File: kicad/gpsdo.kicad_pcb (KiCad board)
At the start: 2 copper layers, 101.6 x 76.2 mm, 9 parts, among them J1 RJ45_Abracon_ARJP11A-MASA-B-A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, J2 Conn_Coaxial, U1 549CAAC000111BBG, U2 MAX-8Q, U3 Si7051-A20, U4 PIC32MX795F512L-80x-PF

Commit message: add ethernet phy
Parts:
- added C2: 100n, Capacitor_SMD:C_0805_2012Metric, F.Cu at (50.8, 39.4)
- added C3: 100n, Capacitor_SMD:C_0805_2012Metric, F.Cu at (39.7, 45.7)
- added C4: 100n, Capacitor_SMD:C_0805_2012Metric, F.Cu at (108.0, 49.5)
- added C5: 100n, Capacitor_SMD:C_0805_2012Metric, F.Cu at (105.4, 49.5)
- added R2: 100, Resistor_SMD:R_0805_2012Metric, F.Cu at (99.1, 54.6)
- added R3: 100, Resistor_SMD:R_0805_2012Metric, F.Cu at (99.1, 50.8)
- added U5: DP83640TVV_NOPB, Package_QFP:LQFP-48_7x7mm_P0.5mm, F.Cu at (86.4, 50.8)
- moved U1 16.9 mm to (51.2, 45.7)
- moved U3 16.9 mm to (45.7, 45.7)
- moved U4 14.8 mm to (64.8, 76.2), turned to 90 degrees
- renumbered C2 to C1
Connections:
- J1 pad 1: Net-(J1-Pad1) -> TD+
- J1 pad 2: Net-(J1-Pad2) -> TD-
- J1 pad 3: Net-(J1-Pad3) -> RD+
- J1 pad 4: Net-(J1-Pad4) -> +3V3
- J1 pad 5: Net-(J1-Pad5) -> +3V3
- J1 pad 6: Net-(J1-Pad6) -> RD-
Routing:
- net RD-: track 0.00 -> 29.3 mm, vias 0 -> 1
- net TD+: track 0.00 -> 26.7 mm, vias 0 -> 2
- net TD-: track 0.00 -> 25.4 mm
- net RD+: track 0.00 -> 21.6 mm
- net +3V3: track 0.00 -> 9.55 mm
- net GND: track 0.00 -> 6.49 mm, vias 43 -> 68

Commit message: board progress
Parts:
- removed the U4 at (64.8, 76.2)
- added R10: 10k, Resistor_SMD:R_0603_1608Metric, F.Cu at (56.0, 78.1)
- added R11: 10k, Resistor_SMD:R_0603_1608Metric, F.Cu at (52.6, 78.1)
- added R12: 10k, Resistor_SMD:R_0603_1608Metric, F.Cu at (56.0, 80.0)
- added R13: 10k, Resistor_SMD:R_0603_1608Metric, F.Cu at (52.6, 80.0)
- added R14: 10k, Resistor_SMD:R_0603_1608Metric, F.Cu at (56.0, 81.9)
- added R15: 10k, Resistor_SMD:R_0603_1608Metric, F.Cu at (52.6, 81.9)
- added R16: 10k, Resistor_SMD:R_0603_1608Metric, F.Cu at (56.0, 83.8)
- added R17: 10k, Resistor_SMD:R_0603_1608Metric, F.Cu at (52.6, 83.8)
- added R18: 10k, Resistor_SMD:R_0603_1608Metric, F.Cu at (56.0, 85.7)
- added R19: 10k, Resistor_SMD:R_0603_1608Metric, F.Cu at (52.6, 85.7)
- added R4: 10k, Resistor_SMD:R_0603_1608Metric, F.Cu at (56.0, 72.4)
- added R5: 10k, Resistor_SMD:R_0603_1608Metric, F.Cu at (52.6, 72.4)
- added R6: 10k, Resistor_SMD:R_0603_1608Metric, F.Cu at (56.0, 74.3)
- added R7: 10k, Resistor_SMD:R_0603_1608Metric, F.Cu at (52.6, 74.3)
- added R8: 10k, Resistor_SMD:R_0603_1608Metric, F.Cu at (56.0, 76.2)
- added R9: 10k, Resistor_SMD:R_0603_1608Metric, F.Cu at (52.6, 76.2)
- added U5: AM3352BZCE60, kicad:BGA298C65P19X19_1300X1300X130, F.Cu at (67.3, 67.3)
- moved C4 7.11 mm to (56.1, 44.1), turned to 270 degrees
- moved C5 6.90 mm to (45.7, 49.1)
- renumbered C4 to C2, C5 to C3, C2 to C4, C3 to C5, J2 to J1, J1 to J2, U3 to U2, U2 to U3, U5 to U4
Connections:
- net Net-(U1-Pad4) renamed CLK_25M
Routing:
- net Net-(U1-Pad7): track 0.00 -> 5.85 mm
- net Net-(U1-Pad8): track 0.00 -> 5.85 mm
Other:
- copper layers 2 -> 4
- rule trace_min: 0.2 -> 0.127
- rule via_min_drill: 0.3 -> 0.254
- rule via_min_size: 0.4 -> 0.508

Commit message: update layout
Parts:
- removed the C3 at (105.4, 49.5)
- removed J2: RJ45_Abracon_ARJP11A-MASA-B-A-EMU2, Connector_RJ:RJ45_Abracon_ARJP11A-MA_Horizontal
- removed R10, R11, R12, R13, R14, R15, R16, R17, R18, R19, R4, R5, R6, R7, R8, R9: 10k, Resistor_SMD:R_0603_1608Metric
- removed R2, R3: 100, Resistor_SMD:R_0805_2012Metric
- removed the U3 at (105.3, 79.2)
- removed the U4 at (86.4, 50.8)
- removed U5: AM3352BZCE60, kicad:BGA298C65P19X19_1300X1300X130
- added C5: 100n, Capacitor_SMD:C_0805_2012Metric, F.Cu at (81.3, 45.5)
- added C6: 100n, Capacitor_SMD:C_0805_2012Metric, F.Cu at (85.7, 42.5)
- added C7: 470n, Capacitor_SMD:C_0805_2012Metric, F.Cu at (81.3, 48.4)
- added U1: MSP430F5171IDA, Package_SO:TSSOP-38_4.4x9.7mm_P0.5mm, F.Cu at (74.9, 46.7)
- added U2: MAX-8Q, RF_GPS:ublox_MAX, F.Cu at (105.3, 36.6)
- moved C1 42.5 mm to (116.8, 35.2)
- moved J1 42.5 mm to (122.3, 39.9)
- moved L1 42.5 mm to (116.8, 39.0)
- moved R1 42.5 mm to (114.6, 37.1)
- moved C2 27.6 mm to (81.3, 42.5), turned to 0 degrees
- renumbered C4 to C3, C5 to C4, U1 to U3, U2 to U4
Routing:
- net RD-: track 29.3 -> 0.00 mm, vias 1 -> 0
- net TD+: track 26.7 -> 0.00 mm, vias 2 -> 0
- net TD-: track 25.4 -> 0.00 mm
- net RD+: track 21.6 -> 0.00 mm
- net +3V3: track 9.55 -> 0.00 mm
- net GND: track 6.49 -> 0.00 mm, vias 68 -> 43

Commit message: update layout
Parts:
- added J2: Conn_01x04_Male, Connector_PinHeader_2.54mm:PinHeader_1x04_P2.54mm_Vertical, F.Cu at (27.9, 27.9)
- added J3: Conn_01x04_Male, Connector_PinHeader_2.54mm:PinHeader_1x04_P2.54mm_Vertical, F.Cu at (46.6, 69.8)
- added J4: Conn_01x04_Male, Connector_PinHeader_2.54mm:PinHeader_1x04_P2.54mm_Vertical, F.Cu at (51.2, 69.8)
- added J5: Conn_01x04_Male, Connector_PinHeader_2.54mm:PinHeader_1x04_P2.54mm_Vertical, F.Cu at (55.9, 69.8)
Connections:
- U1 pad 15: Net-(U1-Pad15) -> gPPS
- U2 pad 4: Net-(U2-Pad4) -> gPPS

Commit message: update board layout
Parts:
- added C10: 10u, Capacitor_SMD:C_0805_2012Metric, F.Cu at (53.9, 34.0)
- added C11: 100n, Resistor_SMD:R_0603_1608Metric, F.Cu at (73.7, 38.1)
- added C8: 100n, Resistor_SMD:R_0603_1608Metric, F.Cu at (73.9, 53.3)
- added C9: 100n, Resistor_SMD:R_0603_1608Metric, F.Cu at (54.1, 30.5)
- added R2: 1.5k, Resistor_SMD:R_0603_1608Metric, F.Cu at (66.8, 44.7)
- added R3: 1.5k, Resistor_SMD:R_0603_1608Metric, F.Cu at (66.8, 46.7)
- added R4: 1.5k, Resistor_SMD:R_0603_1608Metric, F.Cu at (88.7, 31.7)
- added R5: 1.5k, Resistor_SMD:R_0603_1608Metric, F.Cu at (90.4, 31.7)
- added R6: 1.5k, Resistor_SMD:R_0603_1608Metric, F.Cu at (49.8, 42.4)
- added R7: 1.5k, Resistor_SMD:R_0603_1608Metric, F.Cu at (49.8, 38.3)
- added U5: LTC4317, Package_DFN_QFN:DFN-16-1EP_3x5mm_P0.5mm_EP1.66x4.4mm, F.Cu at (73.7, 50.3)
- C1, C2, C3, C4, C5, C6: footprint Capacitor_SMD:C_0805_2012Metric -> Resistor_SMD:R_0603_1608Metric
- L1: footprint Inductor_SMD:L_0805_2012Metric -> Resistor_SMD:R_0603_1608Metric
- R1: footprint Resistor_SMD:R_0805_2012Metric -> Resistor_SMD:R_0603_1608Metric
- moved J5 55.0 mm to (91.4, 27.9), turned to 90 degrees
- moved J4 43.5 mm to (91.4, 53.3), turned to 90 degrees
- moved C6 25.9 mm to (60.2, 38.3), turned to 90 degrees
- moved J1 25.4 mm to (96.8, 39.9)
- moved R1 24.4 mm to (90.2, 36.1), turned to 180 degrees
- moved L1 23.9 mm to (93.0, 39.0)
- moved U2 23.9 mm to (81.4, 36.6)
- moved C1 23.9 mm to (93.0, 35.2)
- moved C7 23.3 mm to (66.9, 30.1), turned to 90 degrees
- moved J2 22.4 mm to (50.3, 27.9)
- moved C2 20.3 mm to (65.0, 30.3), turned to 90 degrees
- moved C5 18.7 mm to (70.3, 30.3), turned to 90 degrees
- moved C3 17.4 mm to (40.9, 35.6), turned to 0 degrees
- moved J3 16.9 mm to (50.3, 53.3), turned to 90 degrees
- moved U1 13.6 mm to (66.3, 36.2), turned to 90 degrees
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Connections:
- net Net-(U1-Pad16) renamed oPPS
- J2 pad 3: GND -> +3V3
- J2 pad 4: GND -> ePPS
- J4 pad 1: GND -> Net-(J4-Pad1)
- J4 pad 2: GND -> Net-(J4-Pad2)
- J5 pad 1: GND -> Net-(J5-Pad1)
- J5 pad 2: GND -> Net-(J5-Pad2)
- U1 pad 17: Net-(U1-Pad17) -> ePPS
- U1 pad 6: Net-(U1-Pad6) -> Net-(J4-Pad1)
- U1 pad 7: Net-(U1-Pad7) -> Net-(J4-Pad2)
- U2 pad 16: Net-(U2-Pad16) -> Net-(R5-Pad1)
- U2 pad 17: Net-(U2-Pad17) -> Net-(R4-Pad2)
- U2 pad 2: Net-(U2-Pad2) -> Net-(J5-Pad1)
- U2 pad 3: Net-(U2-Pad3) -> Net-(J5-Pad2)
- U2 pad 9: Net-(U2-Pad9) -> Net-(U1-Pad19)
- U3 pad 1: Net-(U3-Pad1) -> +3V3
- U3 pad 7: Net-(U2-Pad16) -> Net-(R7-Pad1)
- U3 pad 8: Net-(U2-Pad17) -> Net-(R6-Pad2)
- U4 pad 1: Net-(U2-Pad16) -> Net-(R7-Pad1)
- U4 pad 4: Net-(U4-Pad4) -> +3V3
- U4 pad 6: Net-(U2-Pad17) -> Net-(R6-Pad2)
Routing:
- net Net-(R7-Pad1): track 0.00 -> 46.7 mm, vias 0 -> 4
- net Net-(R6-Pad2): track 0.00 -> 45.2 mm, vias 0 -> 4
- net Net-(J4-Pad2): track 0.00 -> 42.5 mm
- net Net-(J4-Pad1): track 0.00 -> 40.2 mm
- net GND: track 0.00 -> 36.5 mm, vias 43 -> 33
- net Net-(R4-Pad2): track 0.00 -> 29.6 mm, vias 0 -> 2
- net Net-(R5-Pad1): track 0.00 -> 25.3 mm
- net CLK_25M: track 0.00 -> 24.2 mm
- net Net-(U1-Pad23): track 0.00 -> 22.5 mm, vias 0 -> 2
- net Net-(U1-Pad24): track 0.00 -> 22.3 mm, vias 0 -> 2
- net Net-(J5-Pad2): track 0.00 -> 20.5 mm
- net ePPS: track 0.00 -> 19.9 mm, vias 0 -> 4
- net Net-(R3-Pad1): track 0.00 -> 19.8 mm
- net Net-(J5-Pad1): track 0.00 -> 17.0 mm
- net Net-(R2-Pad2): track 0.00 -> 16.7 mm, vias 0 -> 2
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- added copper zone on F.Cu, net +3V3
- removed copper zone on F.Cu, net GND
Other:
- board size 101.6 x 76.2 mm -> 76.2 x 30.5 mm
- copper layers 4 -> 2

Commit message: update pcb layout
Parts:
- added C12: 100n, Resistor_SMD:R_0603_1608Metric, F.Cu at (57.1, 48.7)
- added C13: 100n, Resistor_SMD:R_0603_1608Metric, F.Cu at (62.2, 48.8)
- added C14: 100n, Resistor_SMD:R_0603_1608Metric, F.Cu at (52.1, 48.7)
- added C15: 100n, Resistor_SMD:R_0603_1608Metric, F.Cu at (57.4, 38.3)
- added J6: Conn_01x04_Male, Connector_PinHeader_2.54mm:PinHeader_1x04_P2.54mm_Vertical, F.Cu at (74.4, 27.9)
- added R8: 15k, Resistor_SMD:R_0603_1608Metric, F.Cu at (54.6, 45.0)
- added R9: 15k, Resistor_SMD:R_0603_1608Metric, F.Cu at (59.7, 45.0)
- added U10: 74AUC1G79, Package_TO_SOT_SMD:SOT-23-5, F.Cu at (72.4, 43.4)
- added U6: 74LVC1G08, Package_TO_SOT_SMD:SOT-23-5, F.Cu at (59.7, 48.4)
- added U7: 74LVC1G08, Package_TO_SOT_SMD:SOT-23-5, F.Cu at (54.6, 48.4)
- added U8: 74AUC1G79, Package_TO_SOT_SMD:SOT-23-5, F.Cu at (49.5, 48.4)
- added U9: 74LVC1G86, Package_TO_SOT_SMD:SOT-23-5, F.Cu at (54.7, 38.1)
- moved C10 34.8 mm to (85.9, 47.8)
- moved R7 0.81 mm to (49.8, 39.1)
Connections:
- net Net-(J4-Pad1) renamed /uTXD
- net Net-(J4-Pad2) renamed /uRXD
- net Net-(J5-Pad1) renamed /gTXD
- net Net-(J5-Pad2) renamed /gRXD
- net Net-(R2-Pad2) renamed /SCL
- net Net-(R3-Pad1) renamed /SDA
- net Net-(R4-Pad2) renamed /SCL2
- net Net-(R5-Pad1) renamed /SDA2
- net Net-(R6-Pad2) renamed /SCL1
- net Net-(R7-Pad1) renamed /SDA1
- J2 pad 4: ePPS -> +3V3
- J3 pad 3: GND -> /CLK
- J3 pad 4: GND -> /PPS
- U1 pad 15: gPPS -> oPPS
- U1 pad 16: oPPS -> gPPS
- U1 pad 17: ePPS -> Net-(U1-Pad17)
- U1 pad 18: Net-(U1-Pad18) -> dPPS
- U1 pad 23: Net-(U1-Pad23) -> /EN2
- U1 pad 24: Net-(U1-Pad24) -> /EN1
- U1 pad 25: Net-(U1-Pad25) -> iPPS
- U1 pad 26: Net-(U1-Pad26) -> mPPS
- U1 pad 27: Net-(U1-Pad27) -> gPPS
- U1 pad 35: Net-(U1-Pad35) -> /SBWTCK
- U1 pad 36: Net-(U1-Pad36) -> /SBWTDIO
- U1 pad 5: Net-(U1-Pad5) -> EN_CLK
- U1 pad 8: Net-(U1-Pad8) -> EN_PPS
- U5 pad 2: Net-(U1-Pad23) -> /EN1
- U5 pad 8: Net-(U1-Pad24) -> /EN2
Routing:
- net oPPS: track 0.00 -> 42.8 mm, vias 0 -> 2
- net /SBWTDIO: track 0.00 -> 22.7 mm
- net Net-(U1-Pad23): track 22.5 -> 0.00 mm, vias 2 -> 0
- net Net-(U1-Pad24): track 22.3 -> 0.00 mm, vias 2 -> 0
- net /EN1: track 0.00 -> 21.8 mm, vias 0 -> 2
- net /EN2: track 0.00 -> 21.8 mm, vias 0 -> 2
- net ePPS: track 19.9 -> 0.00 mm, vias 4 -> 0
- net /SBWTCK: track 0.00 -> 19.2 mm
- net mPPS: track 0.00 -> 15.7 mm
- net iPPS: track 0.00 -> 15.3 mm
- net EN_CLK: track 0.00 -> 14.8 mm
- net EN_PPS: track 0.00 -> 12.8 mm, vias 0 -> 2
- net gPPS: track 10.3 -> 21.3 mm, vias 0 -> 2
- net CLK_25M: track 24.2 -> 34.5 mm
- net GND: track 36.5 -> 46.5 mm, vias 33 -> 42
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
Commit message: create gerber files
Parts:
- added R10: 47k, Resistor_SMD:R_0603_1608Metric, F.Cu at (64.0, 26.7)
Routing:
- net /SBWTDIO: track 22.7 -> 23.4 mm

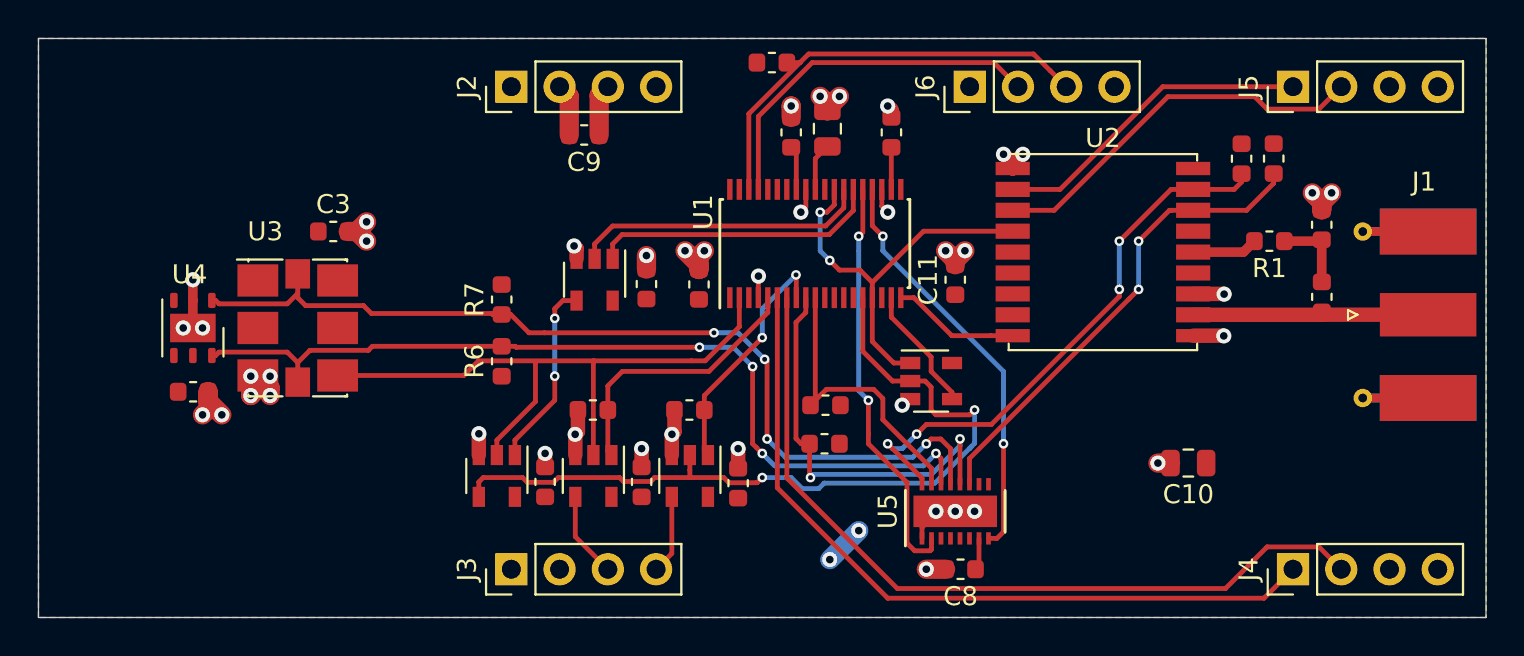
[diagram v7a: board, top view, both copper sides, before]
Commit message: add DCXO shield
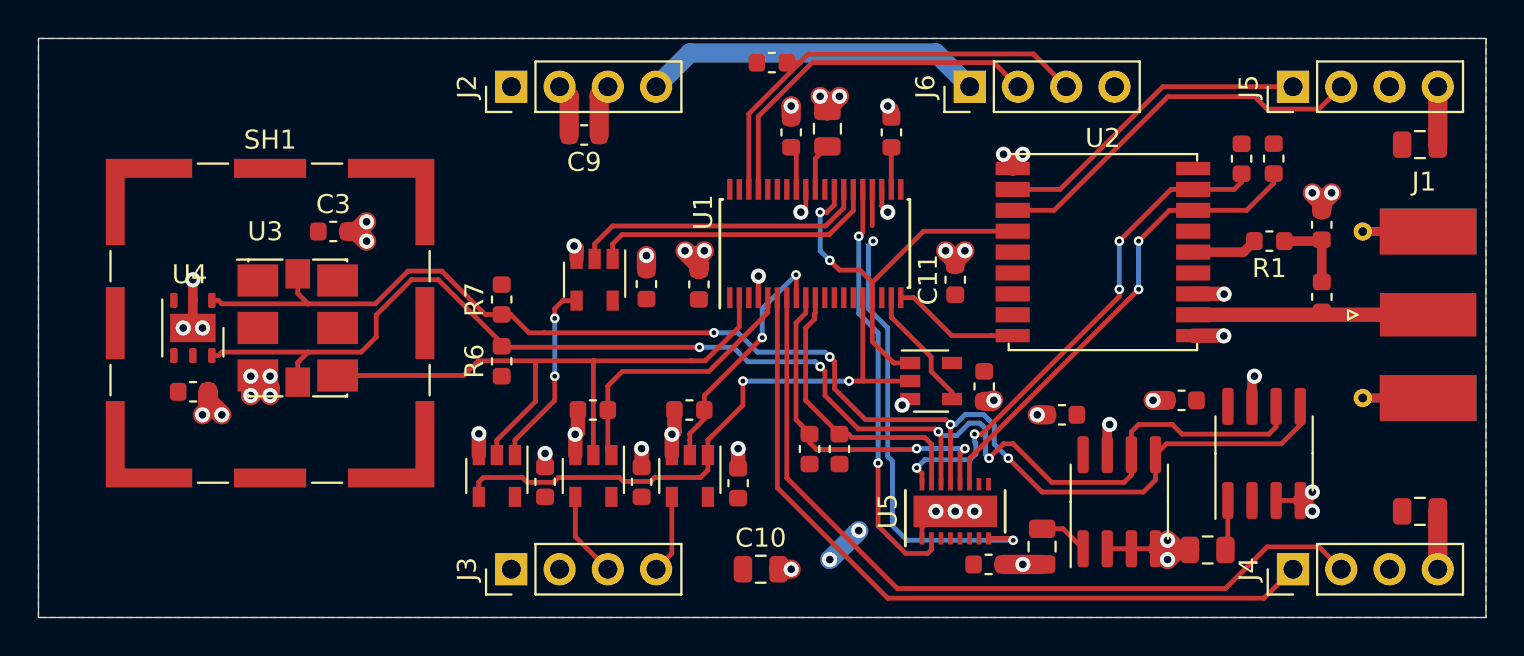
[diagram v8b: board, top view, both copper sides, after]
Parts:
- added C16: 100n, Resistor_SMD:R_0603_1608Metric, F.Cu at (85.6, 44.5)
- added C17: 100n, Resistor_SMD:R_0603_1608Metric, F.Cu at (75.2, 43.7)
- added C18: 100n, Resistor_SMD:R_0603_1608Metric, F.Cu at (79.3, 45.2)
- added C19: 10u, Capacitor_SMD:C_0805_2012Metric, F.Cu at (98.1, 50.3)
- added C20: 10u, Capacitor_SMD:C_0805_2012Metric, F.Cu at (98.1, 31.0)
- added C21: 22u, Capacitor_SMD:C_0805_2012Metric, F.Cu at (78.2, 52.1)
- added C22: 22u, Capacitor_SMD:C_0805_2012Metric, F.Cu at (86.9, 52.3)
- added SH1: DCXO Shield, RF_Shielding:Laird_Technologies_BMI-S-102_16.50x16.50mm, F.Cu at (37.6, 40.4)
- added U11: 47L64, Package_SO:SOIC-8_3.9x4.9mm_P1.27mm, F.Cu at (82.3, 49.8)
- added U12: 47L64, Package_SO:SOIC-8_3.9x4.9mm_P1.27mm, F.Cu at (89.9, 47.2)
- moved C10 23.2 mm to (63.4, 53.3), turned to 0 degrees
- moved R2 2.43 mm to (67.6, 47.0), turned to 90 degrees
- moved C8 1.49 mm to (75.4, 53.1), turned to 0 degrees
- moved R3 0.84 mm to (66.0, 47.0), turned to 270 degrees
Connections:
- U6 pad 1: EN_PPS -> oPPS
- U6 pad 2: oPPS -> EN_PPS
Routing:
- net /SCL1: track 46.8 -> 74.3 mm
- net /SDA1: track 48.8 -> 73.0 mm
- net GND: track 46.5 -> 67.9 mm, vias 42 -> 51
- net +3V3: track 11.1 -> 27.4 mm
- net oPPS: track 42.8 -> 31.9 mm
- net /EN2: track 21.8 -> 25.5 mm
- net /SDA: track 21.6 -> 18.5 mm
- net Net-(C22-Pad2): track 0.00 -> 2.66 mm
- net Net-(C21-Pad2): track 0.00 -> 2.59 mm
- net /SCL2: track 29.6 -> 27.2 mm
